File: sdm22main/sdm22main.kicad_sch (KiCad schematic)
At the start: 13 parts, among them J1 CANConnection, J2 AnalogConnection, J3 AnalogConnection, J4 SerialConnection, J5 SerialConnection, J6 SerialConnection, J7 SerialConnection, J8 AnalogConnection, U1 Teensy4.1, U2 SN65HVD230_CAN_Transceiver, U3 GPS_ADA746, U4 Accelerometer_ADXL335

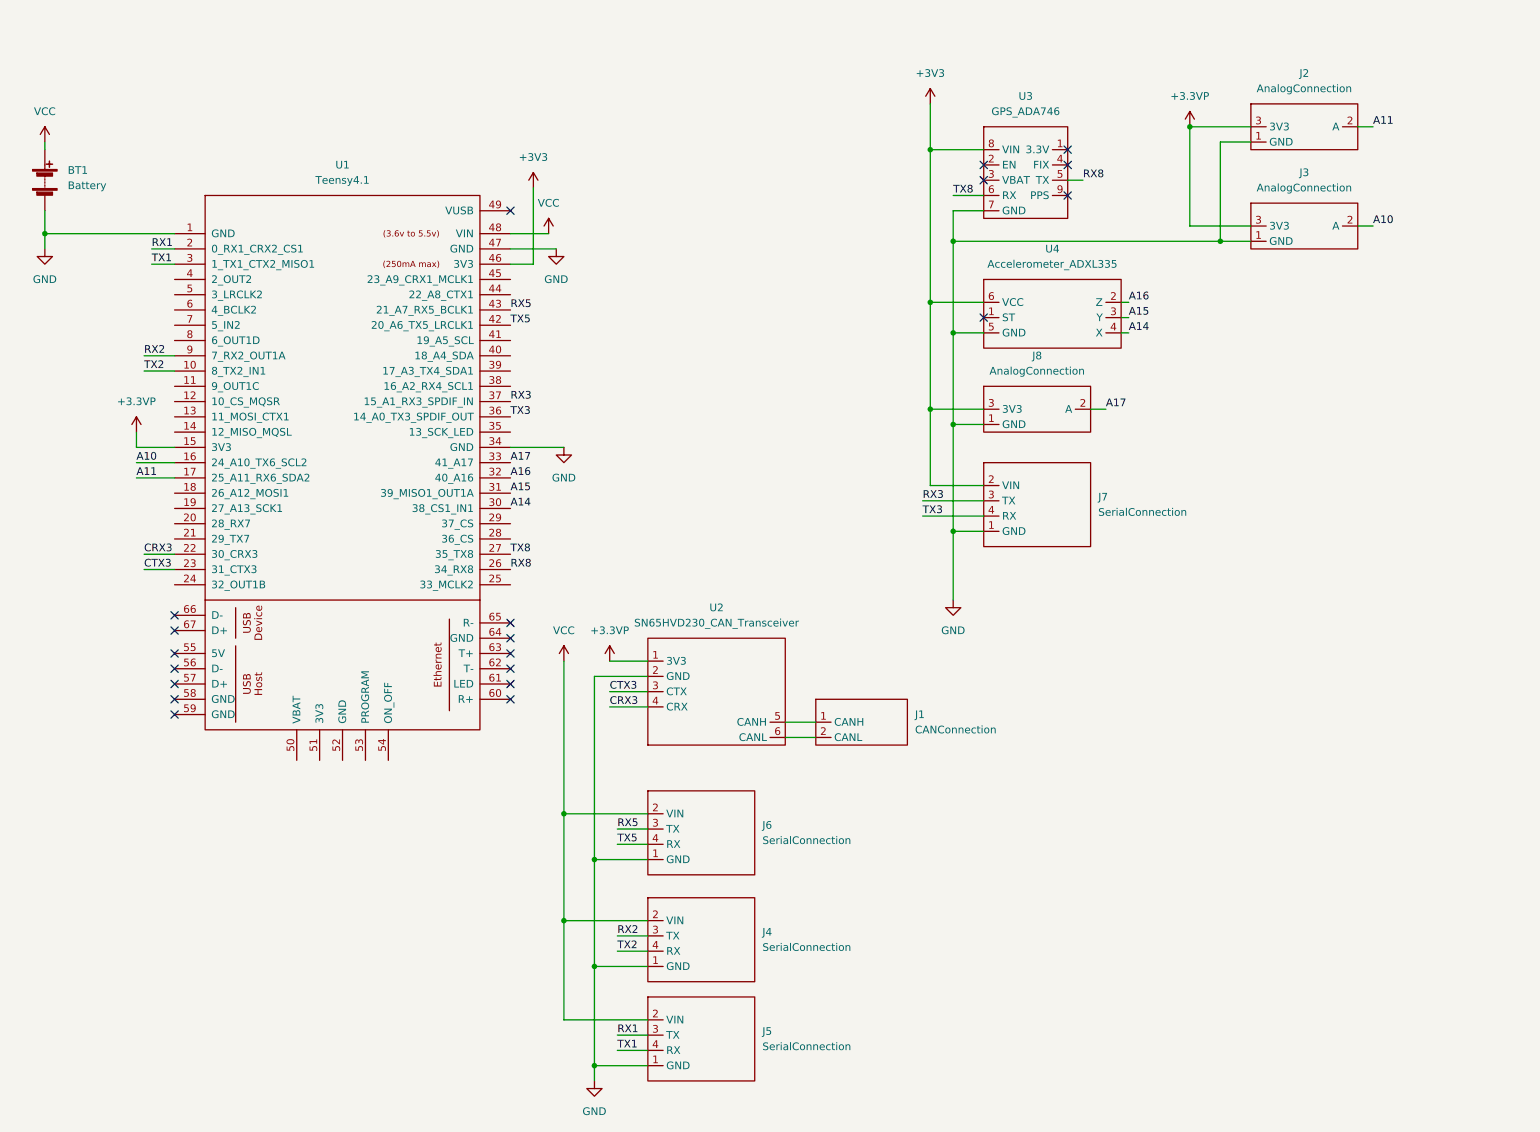
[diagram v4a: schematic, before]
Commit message: added mounting holes, updated battery footprint
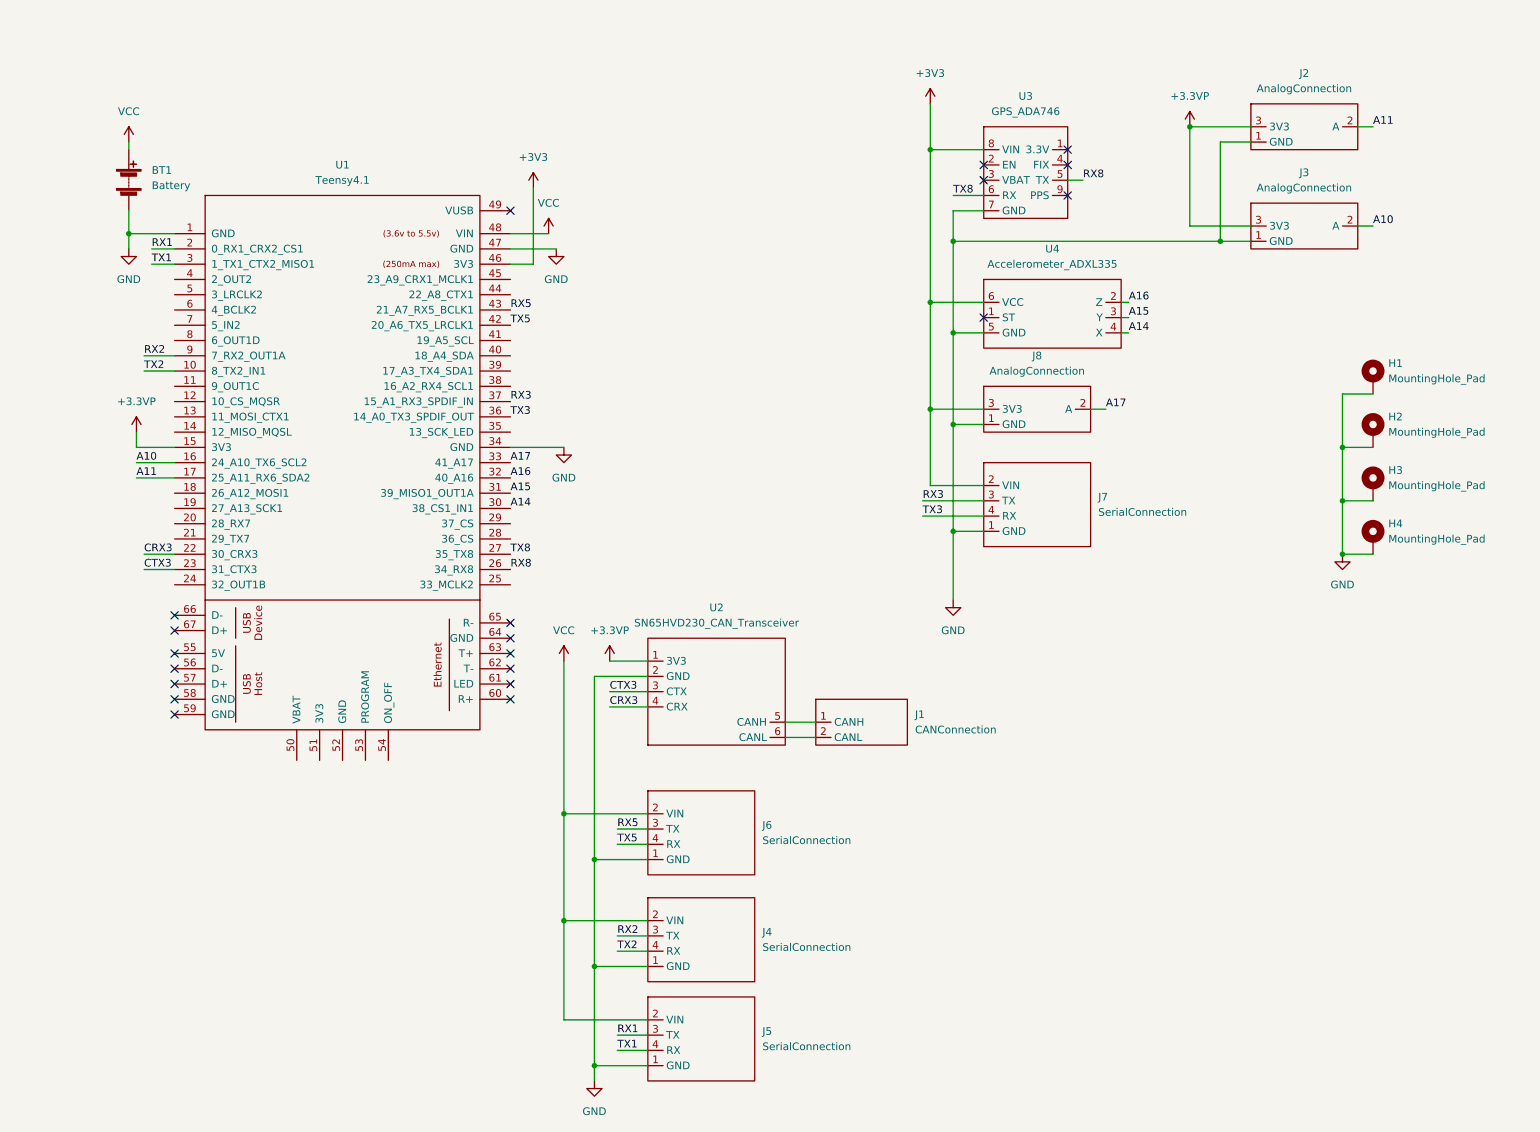
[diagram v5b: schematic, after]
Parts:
- added H1, H2, H3, H4: MountingHole_Pad, MountingHole:MountingHole_3.2mm_M3_ISO7380_Pad, symbol Mechanical:MountingHole_Pad
- BT1: footprint Connector_PinSocket_2.54mm:PinSocket_1x02_P2.54mm_Vertical -> SDM:2Wire_PWRConnector
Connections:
- net GND: now also H1.1, H2.1, H3.1, H4.1
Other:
- moved on the sheet: BT1

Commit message: updated main board with i2c
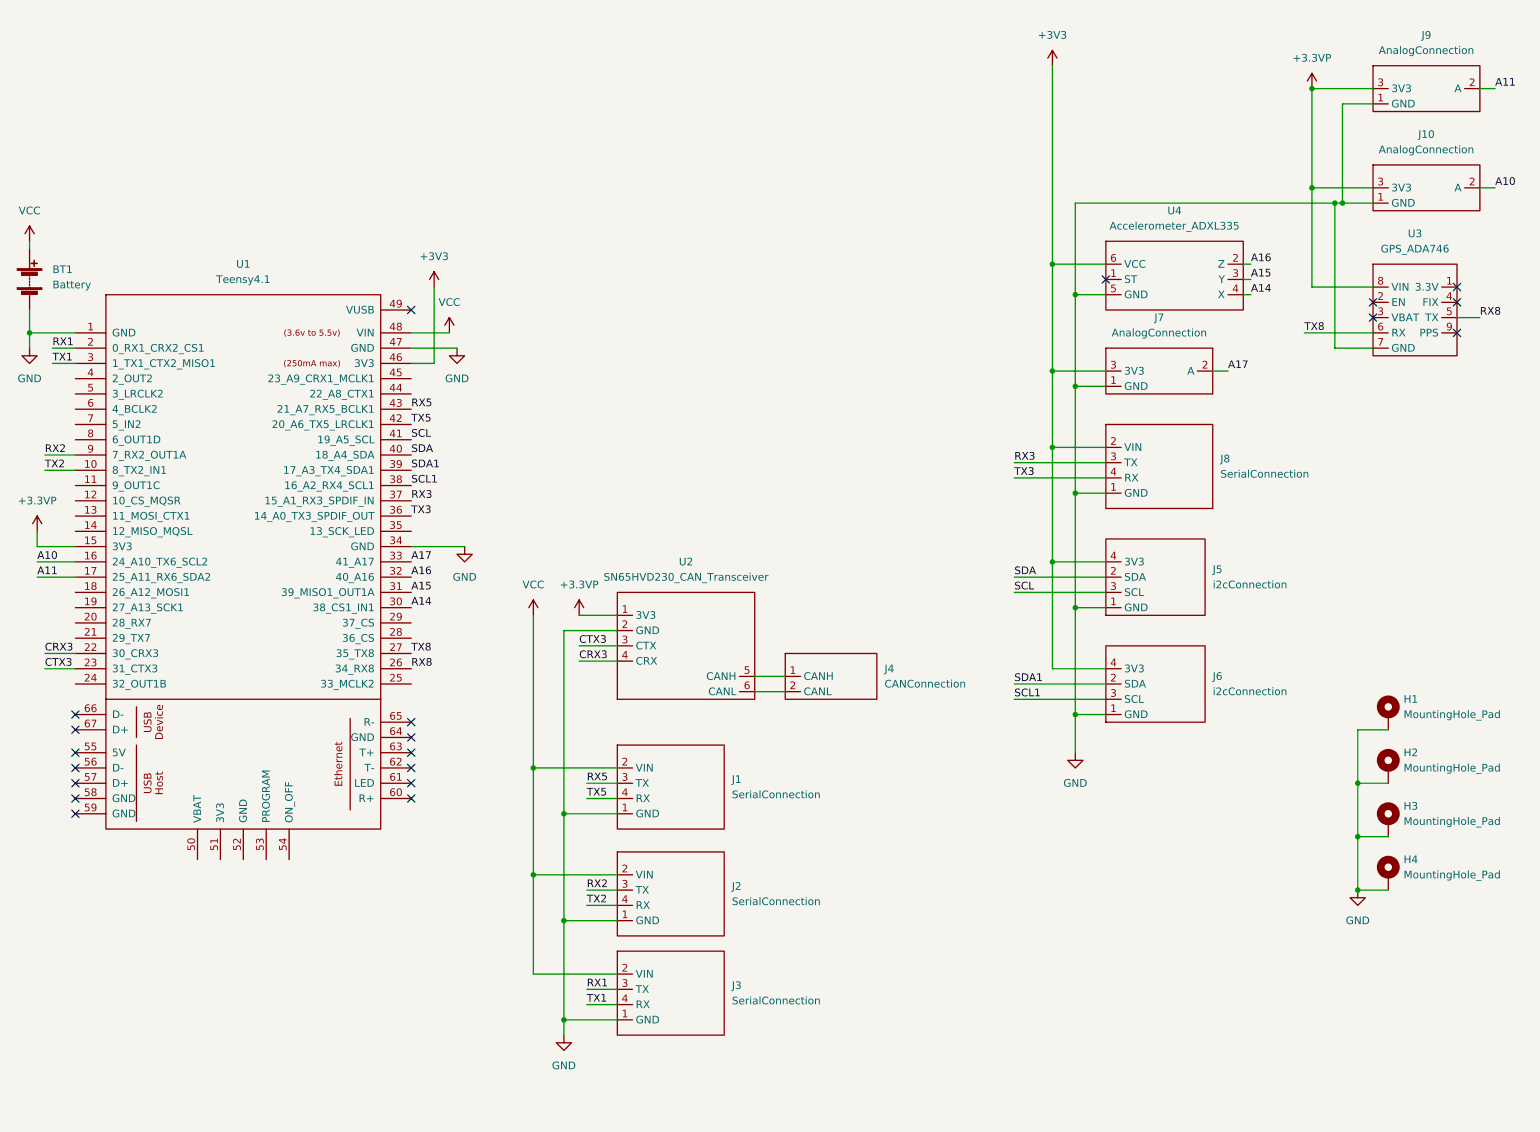
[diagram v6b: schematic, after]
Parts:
- added J5, J6: i2cConnection, SDM:4Wire_i2cConnector, symbol SDM:i2cConnection
- renumbered J6 to J1, J3 to J10, J4 to J2, J5 to J3, J1 to J4, J8 to J7, J7 to J8, J2 to J9
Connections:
- net +3.3VP: now also U3.8 (VIN)
- net +3V3: now also J5.4 (3V3), J6.4 (3V3); no longer U3.8 (VIN)
- net GND: now also J5.1 (GND), J6.1 (GND)
- net SCL1: now reaches U1.38 (16_A2_RX4_SCL1)
- net SCL1: now also J6.3 (SCL)
- net SDA1: now reaches U1.39 (17_A3_TX4_SDA1)
- net SDA1: now also J6.2 (SDA)
- net SDA: now reaches U1.40 (18_A4_SDA)
- net SDA: now also J5.2 (SDA)
- net SCL: now reaches U1.41 (19_A5_SCL)
- net SCL: now also J5.3 (SCL)
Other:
- moved on the sheet: BT1, H1, H2, H3, H4, J1, J10, J2, J3, J4, J7, J8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

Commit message: added extra analog ports to main board
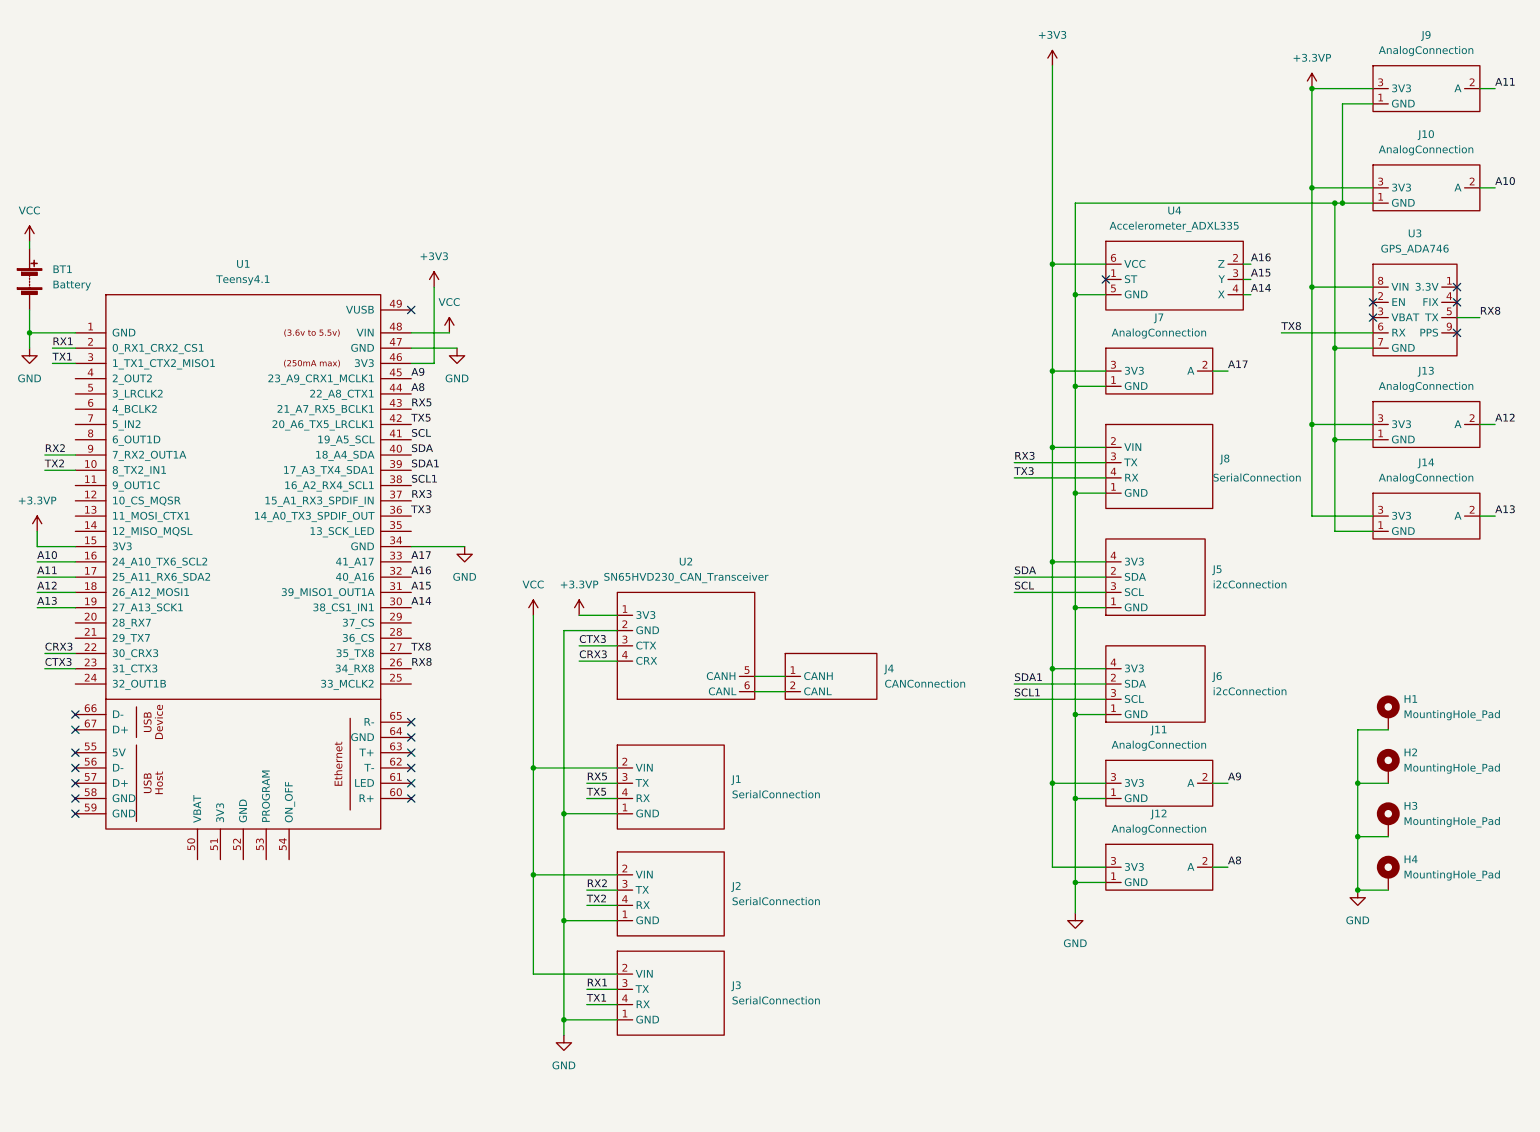
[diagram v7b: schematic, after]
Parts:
- added J11, J12, J13, J14: AnalogConnection, SDM:3Wire_AnalogConnector, symbol SDM:AnalogConnection
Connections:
- net +3.3VP: now also J13.3 (3V3), J14.3 (3V3)
- net +3V3: now also J11.3 (3V3), J12.3 (3V3)
- net GND: now also J11.1 (GND), J12.1 (GND), J13.1 (GND), J14.1 (GND)
- net A12: now reaches U1.18 (26_A12_MOSI1)
- net A12: now also J13.2 (A)
- net A13: now reaches U1.19 (27_A13_SCK1)
- net A13: now also J14.2 (A)
- net A8: now reaches U1.44 (22_A8_CTX1)
- net A8: now also J12.2 (A)
- net A9: now reaches U1.45 (23_A9_CRX1_MCLK1)
- net A9: now also J11.2 (A)

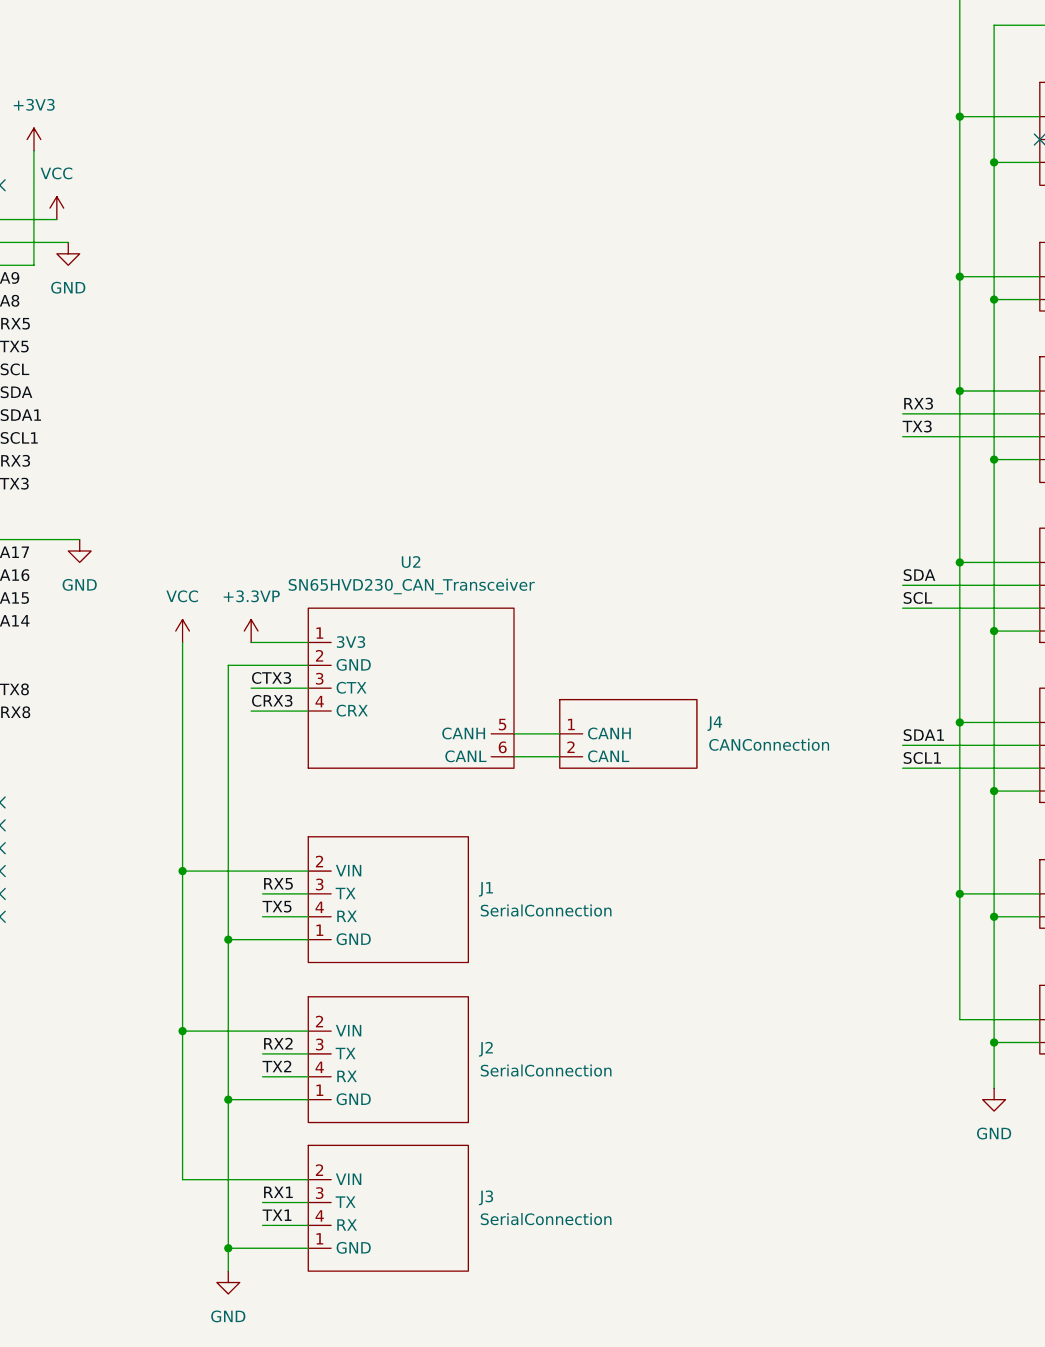
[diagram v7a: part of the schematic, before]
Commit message: checked jlcpcb capabilities against boards
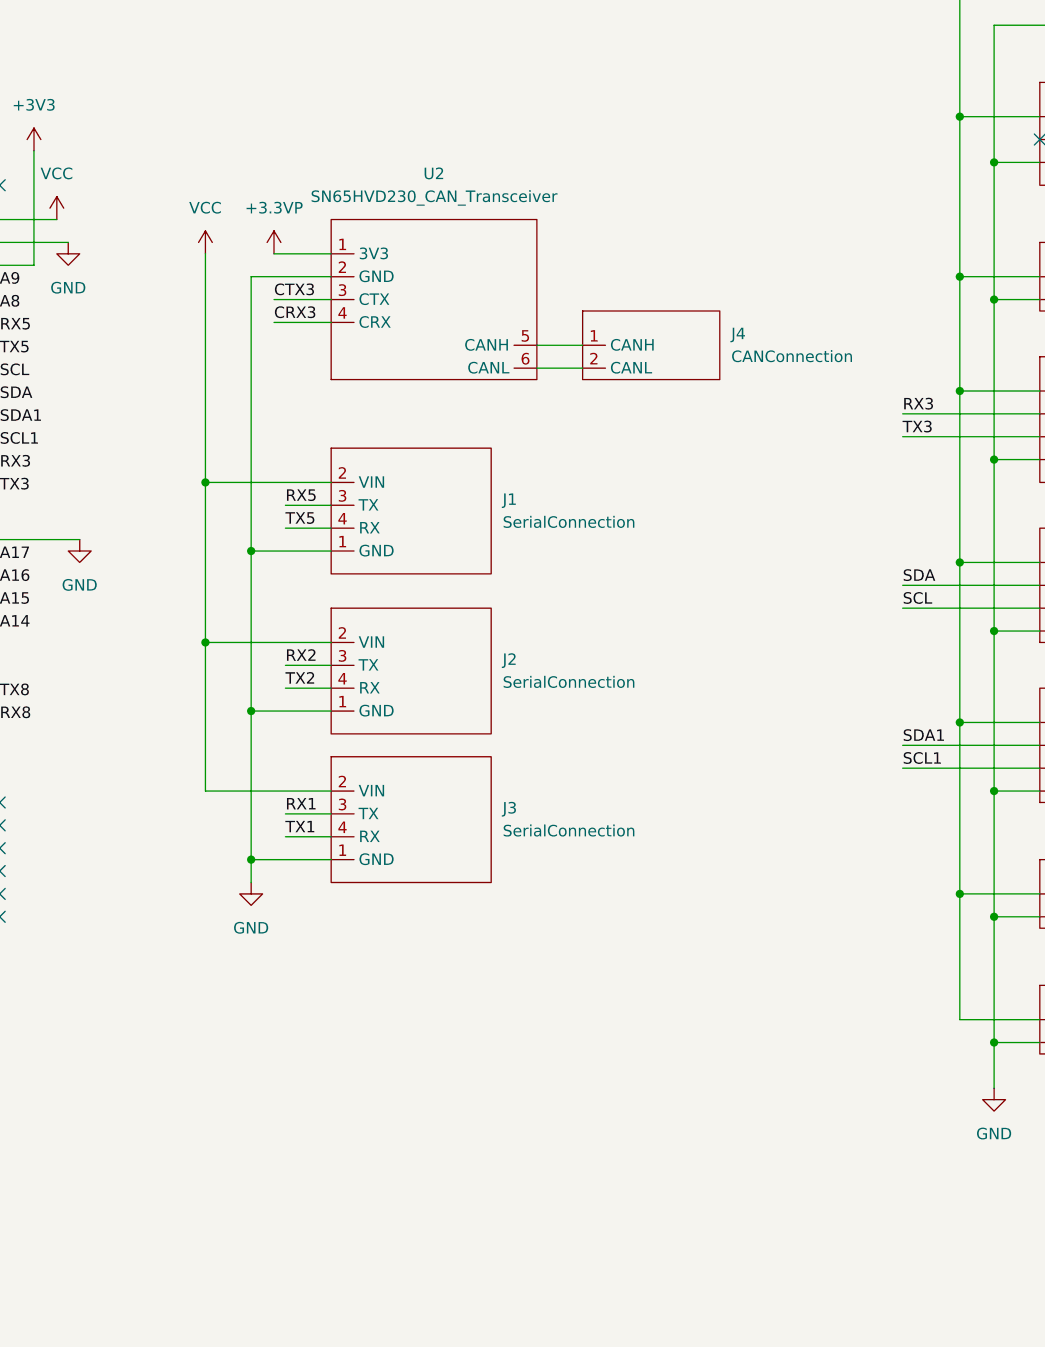
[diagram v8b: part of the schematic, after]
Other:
- moved on the sheet: J1, J2, J3, J4, U2
